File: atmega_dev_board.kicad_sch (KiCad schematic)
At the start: 39 parts, among them J1 1x15 Pin Header, J2 U263-163N-4BLS1735, J3 1x15 Pin Header, J4 2x3 Pin Header, SW1 TS-1187A-B-A-B, SW2 TS-1187A-B-A-B, U1 78L05G-AB3-R, U2 HT7533-1, U3 ATmega328P-A, U4 CP2102N-Axx-xQFN28, Y1 X322516MLB4SI

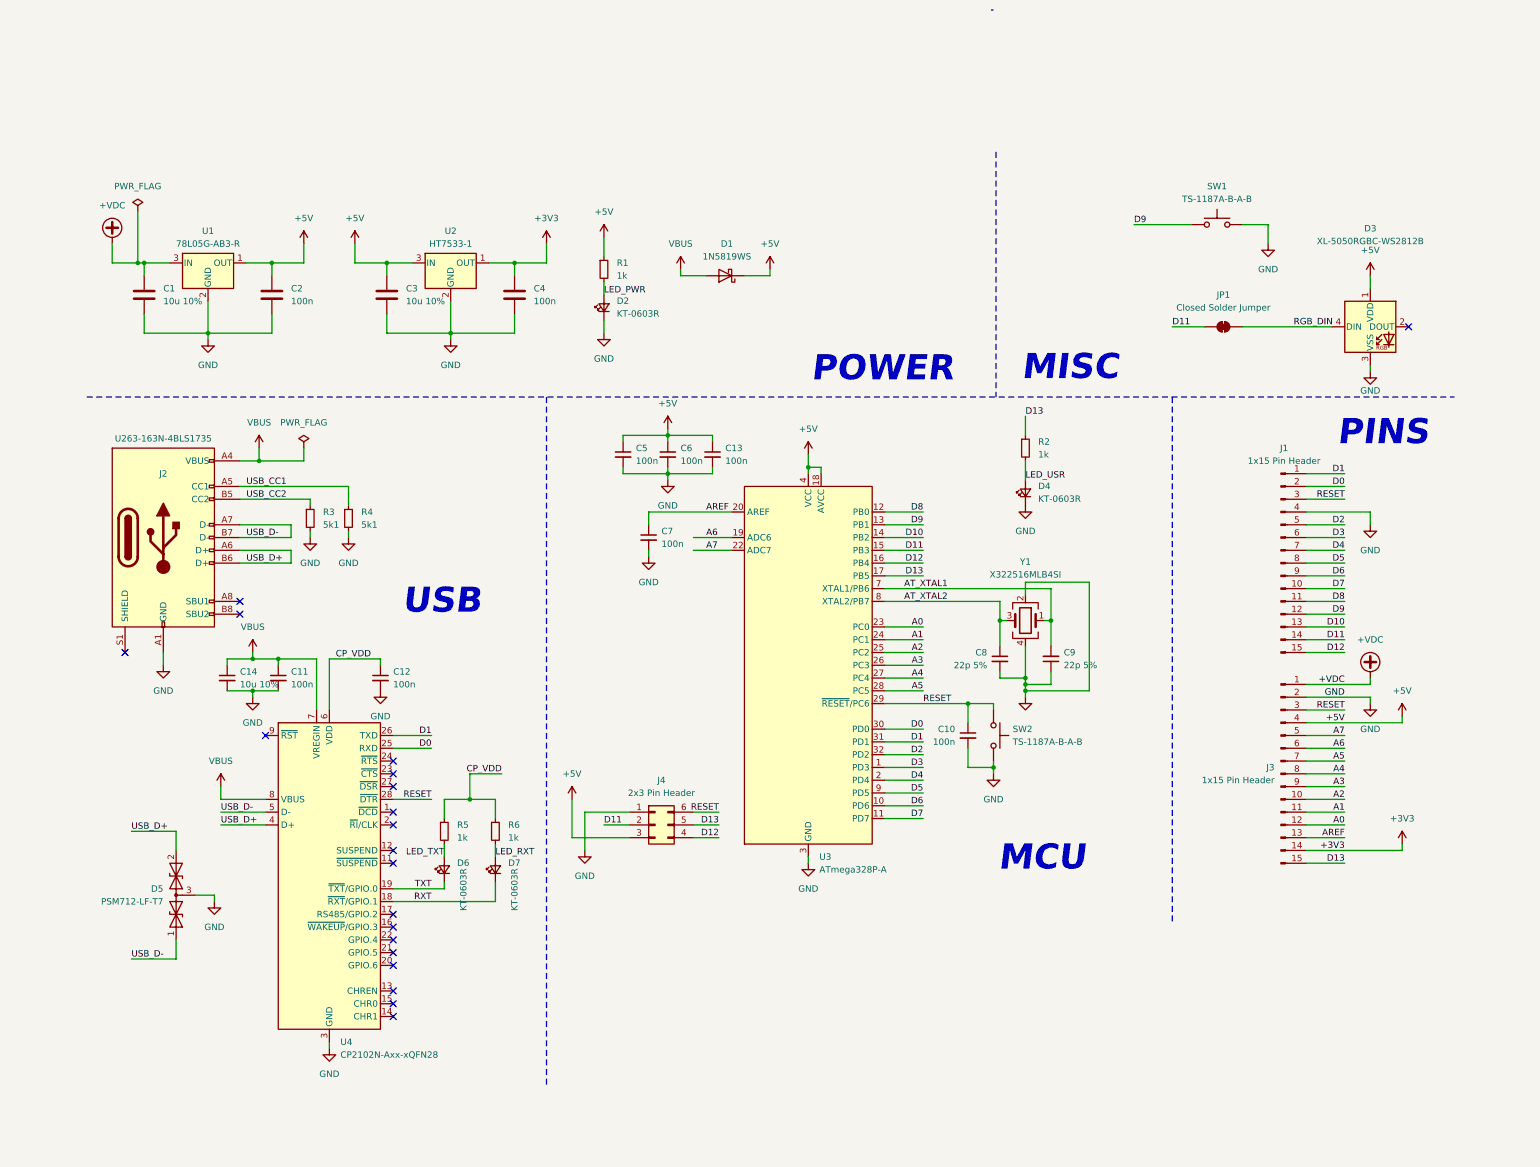
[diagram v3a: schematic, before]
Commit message: Tidy up schema and route all but GPIO traces
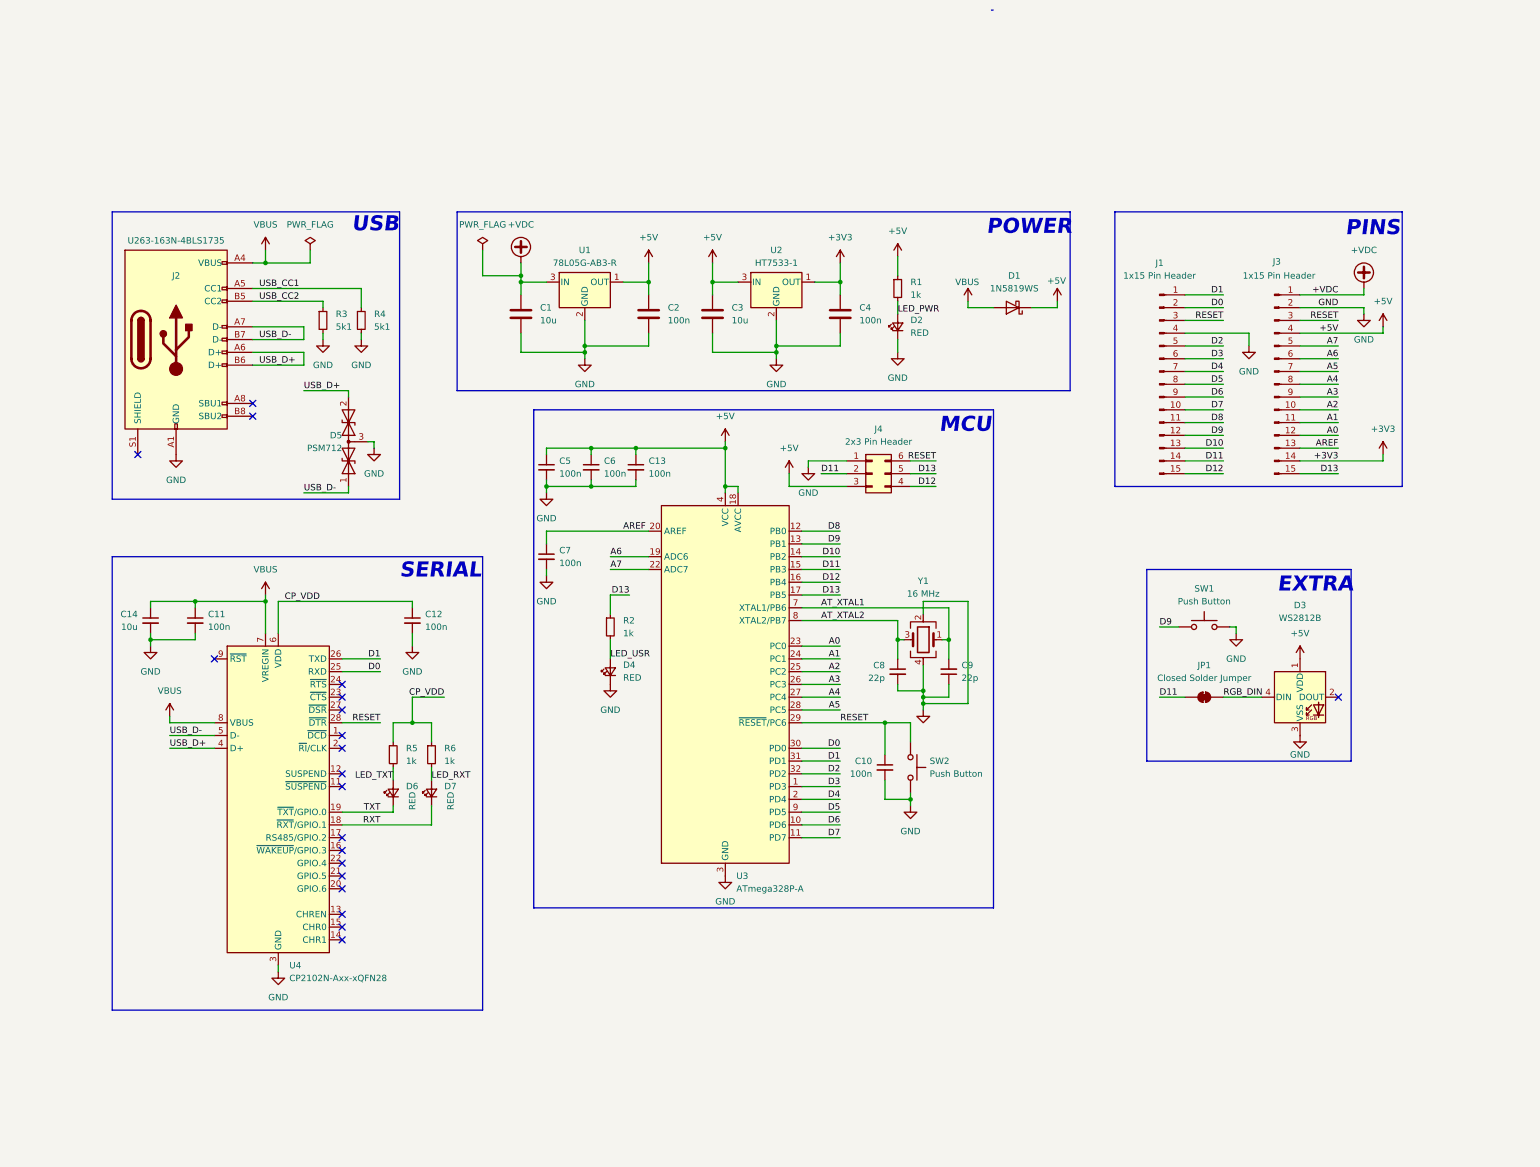
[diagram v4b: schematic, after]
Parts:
- C1, C14, C3: value 10u 10% -> 10u
- C8, C9: value 22p 5% -> 22p
- D2, D4, D6, D7: value KT-0603R -> RED
- D3: value XL-5050RGBC-WS2812B -> WS2812B
- D5: value PSM712-LF-T7 -> PSM712
- SW1, SW2: value TS-1187A-B-A-B -> Push Button
- Y1: value X322516MLB4SI -> 16 MHz
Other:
- note added: "EXTRA"
- note added: "SERIAL"
- note removed: "MISC"
- moved on the sheet: C1, C10, C11, C12, C13, C14, C2, C3, C4, C5, C6, C7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
